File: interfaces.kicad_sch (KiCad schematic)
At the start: 118 parts, among them J6001 HDMI-A_WE_685119134923, J6002 USB-C_USB4105-GF-A, J6003 MicroSD_693071020811, Q6001 BSS138PW, Q6002 BSS138PW, Q6003 BSS138PW, Q6004 BSS138PW, Q6005 BSS138PW, Q6006 BSS138PW, Q6007 BSS138PW, Q6008 BSS138PW, SW6001 SW_KMR211NGLFS_SMD, U6001 FT4232H_VQFN, Y6001 Oscillator_SMD_12MHz_KX-7

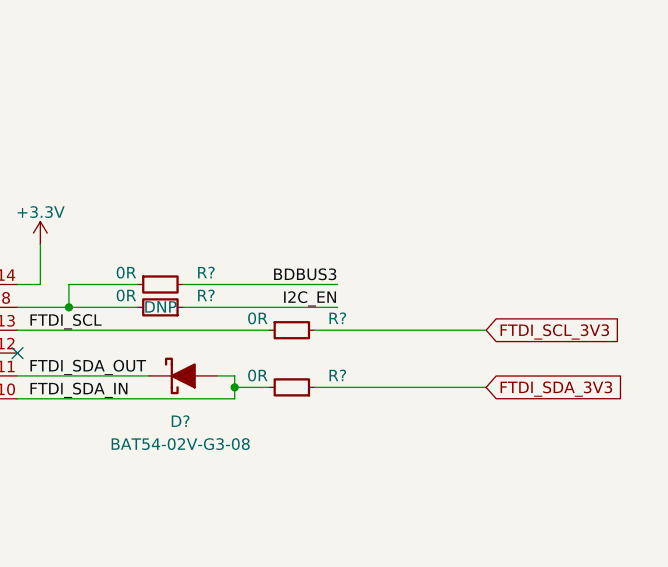
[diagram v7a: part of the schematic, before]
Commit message: Connect control and misc. signals, fix PCIe directions, rework I2C architecture, optimize DC-DC supply utilization
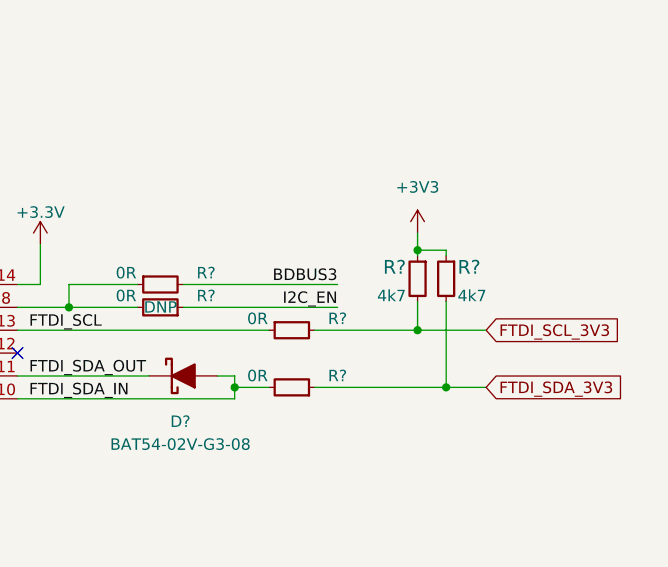
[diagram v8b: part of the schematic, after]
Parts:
- added R? (x2): R_4k7_0402, sodimm-ddr5-tester-footprints:R_0402_1005Metric, symbol sodimm-ddr5-tester:R_4k7_0402
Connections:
- net +3V3: now also R?.1, R?.1
- net FTDI_SCL_3V3: now also R?.2
- net FTDI_SDA_3V3: now also R?.2
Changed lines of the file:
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@@
   (junction (at 321.945 149.86) (diameter 0) (color 0 0 0 0)
   )
+  (junction (at 445.77 339.09) (diameter 0) (color 0 0 0 0)
+  )
   (junction (at 78.74 57.15) (diameter 0) (color 0 0 0 0)
   )
@@
   (junction (at 55.245 74.295) (diameter 0) (color 0 0 0 0)
   )
+  (junction (at 445.77 347.98) (diameter 0) (color 0 0 0 0)
+  )
   (junction (at 259.08 261.62) (diameter 0) (color 0 0 0 0)
   )
@@
   (junction (at 298.45 88.265) (diameter 0) (color 0 0 0 0)
   )
+  (junction (at 448.945 354.33) (diameter 0) (color 0 0 0 0)
+  )
   (junction (at 229.87 152.4) (diameter 0) (color 0 0 0 0)
   )
@@
     (stroke (width 0) (type default) (color 0 0 0 0))
   )
+  (wire (pts (xy 445.77 337.185) (xy 445.77 339.09))
+    (stroke (width 0) (type default) (color 0 0 0 0))
+  )
   (wire (pts (xy 41.275 66.04) (xy 41.275 63.5))
     (stroke (width 0) (type default) (color 0 0 0 0))
@@
     (stroke (width 0) (type default) (color 0 0 0 0))
   )
+  (wire (pts (xy 445.77 339.09) (xy 448.945 339.09))
+    (stroke (width 0) (type default) (color 0 0 0 0))
+  )
   (wire (pts (xy 111.76 158.75) (xy 111.76 161.29))
     (stroke (width 0) (type default) (color 0 0 0 0))
@@
     (stroke (width 0) (type default) (color 0 0 0 0))
   )
-  (wire (pts (xy 434.34 347.98) (xy 453.39 347.98))
+  (wire (pts (xy 434.34 347.98) (xy 445.77 347.98))
     (stroke (width 0) (type default) (color 0 0 0 0))
   )
@@
     (stroke (width 0) (type default) (color 0 0 0 0))
   )
+  (wire (pts (xy 445.77 347.98) (xy 453.39 347.98))
+    (stroke (width 0) (type default) (color 0 0 0 0))
+  )
   (wire (pts (xy 315.595 149.86) (xy 321.945 149.86))
     (stroke (width 0) (type default) (color 0 0 0 0))
@@
     (stroke (width 0) (type default) (color 0 0 0 0))
   )
+  (wire (pts (xy 448.945 354.33) (xy 453.39 354.33))
+    (stroke (width 0) (type default) (color 0 0 0 0))
+  )
   (wire (pts (xy 63.5 87.63) (xy 72.39 87.63))
     (stroke (width 0) (type default) (color 0 0 0 0))
@@
     (stroke (width 0) (type default) (color 0 0 0 0))
   )
-  (wire (pts (xy 434.34 354.33) (xy 453.39 354.33))
+  (wire (pts (xy 434.34 354.33) (xy 448.945 354.33))
     (stroke (width 0) (type default) (color 0 0 0 0))
   )
@@
     (stroke (width 0) (type default) (color 0 0 0 0))
   )
+  (wire (pts (xy 445.77 339.725) (xy 445.77 339.09))
+    (stroke (width 0) (type default) (color 0 0 0 0))
+  )
   (wire (pts (xy 382.27 350.52) (xy 382.27 358.14))
     (stroke (width 0) (type default) (color 0 0 0 0))
@@
     (stroke (width 0) (type default) (color 0 0 0 0))
   )
+  (wire (pts (xy 445.77 344.805) (xy 445.77 347.98))
+    (stroke (width 0) (type default) (color 0 0 0 0))
+  )
   (wire (pts (xy 334.645 160.02) (xy 334.645 177.165))
     (stroke (width 0) (type default) (color 0 0 0 0))
   )
+  (wire (pts (xy 448.945 339.09) (xy 448.945 339.725))
+    (stroke (width 0) (type default) (color 0 0 0 0))
+  )
   (wire (pts (xy 80.645 215.9) (xy 83.185 215.9))
     (stroke (width 0) (type default) (color 0 0 0 0))
@@
     (stroke (width 0) (type default) (color 0 0 0 0))
   )
+  (wire (pts (xy 448.945 344.805) (xy 448.945 354.33))
+    (stroke (width 0) (type default) (color 0 0 0 0))
+  )
   (polyline (pts (xy 299.72 121.285) (xy 299.72 252.73))
     (stroke (width 0) (type default) (color 0 0 0 0))
@@
     (pin "1")
   )
+  (symbol (lib_id "sodimm-ddr5-tester:R_4k7_0402") (at 445.77 339.725 270) (unit 1)
+    (in_bom yes) (on_board yes)
+    (property "Reference" "R?" (id 0) (at 444.5 340.995 90)
+      (effects (font (size 1.524 1.524)) (justify right))
+    )
+    (property "Value" "R_4k7_0402" (id 1) (at 433.07 360.045 0)
+      (effects (font (size 1.27 1.27) (thickness 0.15)) (justify left bottom) hide)
+    )
+    (property "Footprint" "sodimm-ddr5-tester-footprints:R_0402_1005Metric" (id 2) (at 430.53 360.045 0)
+      (effects (font (size 1.27 1.27) (thickness 0.15)) (justify left bottom) hide)
+    )
+    (property "Datasheet" "https://www.bourns.com/docs/product-datasheets/cr.pdf" (id 3) (at 427.99 360.045 0)
+      (effects (font (size 1.27 1.27) (thickness 0.15)) (justify left bottom) hide)
+    )
+    (property "Manufacturer" "Bourns" (id 4) (at 422.91 360.045 0)
+      (effects (font (size 1.27 1.27) (thickness 0.15)) (justify left bottom) hide)
+    )
+    (property "MPN" "CR0402-FX-4701GLF" (id 5) (at 425.45 360.045 0)
+      (effects (font (size 1.27 1.27) (thickness 0.15)) (justify left bottom) hide)
+    )
+    (property "Val" "4k7" (id 6) (at 444.5 344.17 90)
+      (effects (font (size 1.27 1.27) (thickness 0.15)) (justify right))
+    )
+    (property "License" "Apache-2.0" (id 7) (at 420.37 360.045 0)
+      (effects (font (size 1.27 1.27) (thickness 0.15)) (justify left bottom) hide)
+    )
+    (property "Author" "Antmicro" (id 8) (at 417.83 360.045 0)
+      (effects (font (size 1.27 1.27) (thickness 0.15)) (justify left bottom) hide)
+    )
+    (property "Tolerance" "1%" (id 9) (at 435.61 360.045 0)
+      (effects (font (size 1.27 1.27)) (justify left bottom) hide)
+    )
+    (pin "1")
+    (pin "2")
+  )
   (symbol (lib_id "sodimm-ddr5-tester:GND1") (at 387.35 101.6 0) (unit 1)
     (in_bom yes) (on_board yes) (fields_autoplaced)
@@
     (pin "1")
   )
+  (symbol (lib_id "sodimm-ddr5-tester:+3V3") (at 445.77 337.185 0) (unit 1)
+    (in_bom yes) (on_board yes) (fields_autoplaced)
+    (property "Reference" "#PWR?" (id 0) (at 445.77 340.995 0)
+      (effects (font (size 1.27 1.27)) hide)
+    )
+    (property "Value" "+3V3" (id 1) (at 445.77 332.105 0))
+    (property "Footprint" "" (id 2) (at 445.77 337.185 0)
+      (effects (font (size 1.27 1.27)) hide)
+    )
+    (property "Datasheet" "" (id 3) (at 445.77 337.185 0)
+      (effects (font (size 1.27 1.27)) hide)
+    )
+    (pin "1")
+  )
   (symbol (lib_id "antmicroLogicShiftRegisters:SN74HC595B") (at 292.735 347.98 0) (mirror y) (unit 1)
     (in_bom yes) (on_board yes) (fields_autoplaced)
@@
     (pin "1")
   )
+  (symbol (lib_id "sodimm-ddr5-tester:R_4k7_0402") (at 448.945 339.725 270) (unit 1)
+    (in_bom yes) (on_board yes)
+    (property "Reference" "R?" (id 0) (at 450.215 340.995 90)
+      (effects (font (size 1.524 1.524)) (justify left))
+    )
+    (property "Value" "R_4k7_0402" (id 1) (at 436.245 360.045 0)
+      (effects (font (size 1.27 1.27) (thickness 0.15)) (justify left bottom) hide)
+    )
+    (property "Footprint" "sodimm-ddr5-tester-footprints:R_0402_1005Metric" (id 2) (at 433.705 360.045 0)
+      (effects (font (size 1.27 1.27) (thickness 0.15)) (justify left bottom) hide)
+    )
+    (property "Datasheet" "https://www.bourns.com/docs/product-datasheets/cr.pdf" (id 3) (at 431.165 360.045 0)
+      (effects (font (size 1.27 1.27) (thickness 0.15)) (justify left bottom) hide)
+    )
+    (property "Manufacturer" "Bourns" (id 4) (at 426.085 360.045 0)
+      (effects (font (size 1.27 1.27) (thickness 0.15)) (justify left bottom) hide)
+    )
+    (property "MPN" "CR0402-FX-4701GLF" (id 5) (at 428.625 360.045 0)
+      (effects (font (size 1.27 1.27) (thickness 0.15)) (justify left bottom) hide)
+    )
+    (property "Val" "4k7" (id 6) (at 450.215 344.17 90)
+      (effects (font (size 1.27 1.27) (thickness 0.15)) (justify left))
+    )
+    (property "License" "Apache-2.0" (id 7) (at 423.545 360.045 0)
+      (effects (font (size 1.27 1.27) (thickness 0.15)) (justify left bottom) hide)
+    )
+    (property "Author" "Antmicro" (id 8) (at 421.005 360.045 0)
+      (effects (font (size 1.27 1.27) (thickness 0.15)) (justify left bottom) hide)
+    )
+    (property "Tolerance" "1%" (id 9) (at 438.785 360.045 0)
+      (effects (font (size 1.27 1.27)) (justify left bottom) hide)
+    )
+    (pin "1")
+    (pin "2")
+  )
   (symbol (lib_id "antmicroTVSDiodes:TPD4E05U06QDQARQ1") (at 332.74 85.725 0) (unit 1)
